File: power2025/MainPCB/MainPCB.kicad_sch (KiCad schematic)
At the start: 11 parts, among them Q1 SUD08P06-155L, U1 NCP167BMX330TBG

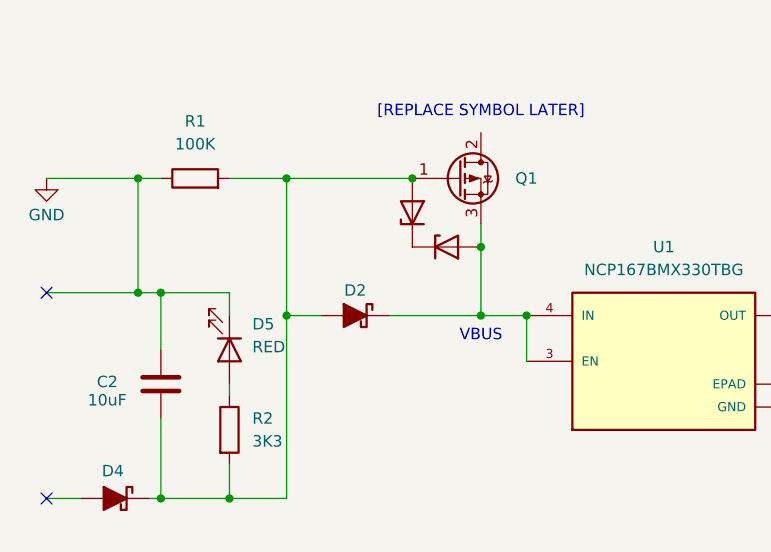
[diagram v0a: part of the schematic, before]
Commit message: Created symbol for CJ3139K mosfet
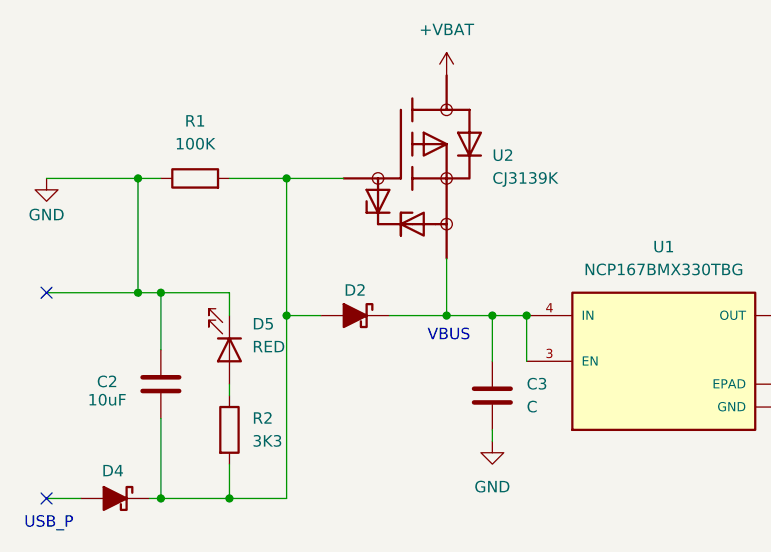
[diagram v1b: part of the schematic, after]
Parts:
- removed D1, D3: D_Zener, symbol Device:D_Zener
- removed Q1: SUD08P06-155L, Package_TO_SOT_SMD:TO-252-2, symbol Transistor_FET:SUD08P06-155L
- added C3: C, symbol Device:C
- added U2: CJ3139K, symbol Added Parts:CJ3139K
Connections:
- net GND: now also C3.2
- net at D2.1 (K), U1.3 (EN), U1.4 (IN): now also C3.1, U2. (S)
- net at C2.2, D2.2 (A), D4.1 (K)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: now also U2. (S)
- new net +VBAT: U2. (S)
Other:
- note added: "USB_P"
- note removed: "[REPLACE SYMBOL LATER]"

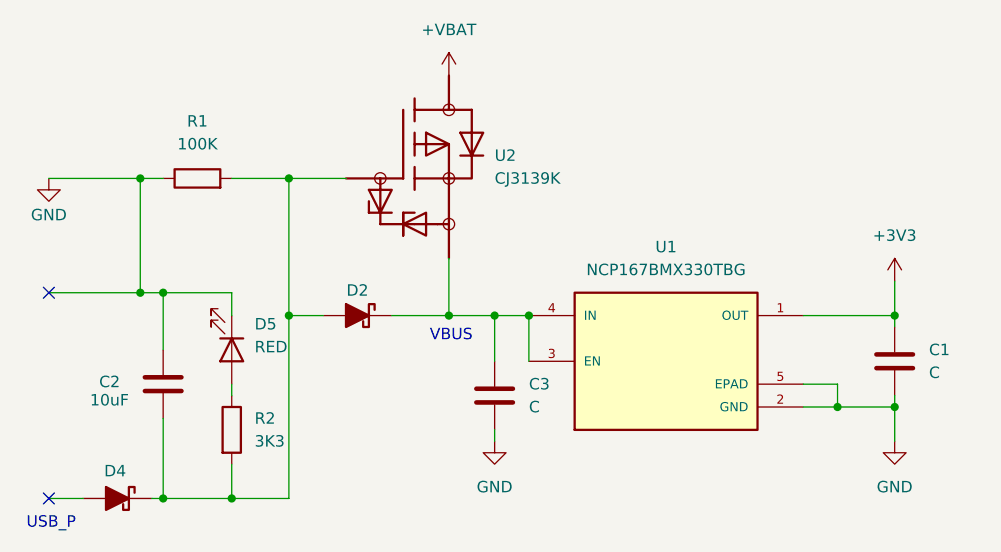
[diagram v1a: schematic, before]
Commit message: Added specific values for in/out capacitors
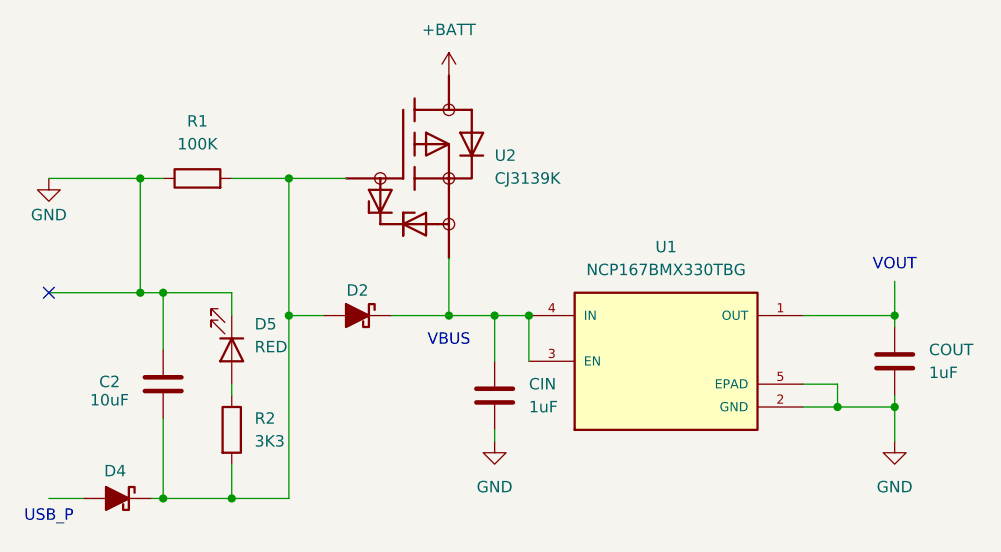
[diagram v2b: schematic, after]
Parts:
- CIN: renamed from C3; value C -> 1uF
- COUT: renamed from C1; value C -> 1uF
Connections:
- net +3V3: no longer names the net of COUT.1, U1.1 (OUT)
- net +VBAT renamed +BATT
- no-connect marks 2 -> 1
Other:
- note added: "VOUT"
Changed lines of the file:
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@@
 	(generator_version "9.0")
 	(paper "A4")
-	(text "USB_P"
-		(exclude_from_sim no)
-		(at 52.324 70.104 0)
+	(text "VOUT"
+		(exclude_from_sim no)
+		(at 146.05 41.402 0)
 		(effects
 			(font
 				(size 1.27 1.27)
-				(color 0 0 0 1)
 			)
 		)
@@
 	(text "VBUS"
 		(exclude_from_sim no)
-		(at 96.774 49.276 0)
+		(at 96.52 49.784 0)
 		(effects
 			(font
 				(size 1.27 1.27)
-				(color 0 0 0 1)
+			)
+		)
+	)
+	(text "USB_P\n"
+		(exclude_from_sim no)
+		(at 52.07 69.342 0)
+		(effects
+			(font
+				(size 1.27 1.27)
 			)
 		)
@@
 	(no_connect
 		(at 52.07 44.45)
-	)
-	(no_connect
-		(at 52.07 67.31)
 	)
 	(wire
@@
 		(dnp no)
 		(fields_autoplaced yes)
-		(property "Reference" "C1"
+		(property "Reference" "COUT"
 			(at 149.86 50.7999 0)
 			(effects
@@
 			)
 		)
-		(property "Value" "C"
+		(property "Value" "1uF"
 			(at 149.86 53.3399 0)
 			(effects
@@
 			(project ""
 				(path "/352d37ed-eb7c-4d4e-9251-f506b387d60c"
-					(reference "C1")
+					(reference "COUT")
 					(unit 1)
 				)
@@
 		(dnp no)
 		(fields_autoplaced yes)
-		(property "Reference" "#PWR04"
+		(property "Reference" "#PWR02"
 			(at 96.52 24.13 0)
 			(effects
@@
 			)
 		)
-		(property "Value" "+VBAT"
+		(property "Value" "+BATT"
 			(at 96.52 15.24 0)
 			(effects
@@
 			(project ""
 				(path "/352d37ed-eb7c-4d4e-9251-f506b387d60c"
-					(reference "#PWR04")
+					(reference "#PWR02")
 					(unit 1)
 				)
@@
 		(dnp no)
 		(fields_autoplaced yes)
-		(property "Reference" "C3"
+		(property "Reference" "CIN"
 			(at 105.41 54.6099 0)
 			(effects
@@
 			)
 		)
-		(property "Value" "C"
+		(property "Value" "1uF"
 			(at 105.41 57.1499 0)
 			(effects
@@
 			(project "MainPCB"
 				(path "/352d37ed-eb7c-4d4e-9251-f506b387d60c"
-					(reference "C3")
+					(reference "CIN")
 					(unit 1)
 				)
-			)
-		)
-	)
-	(symbol
-		(lib_id "power:+3V3")
-		(at 146.05 43.18 0)
-		(unit 1)
-		(exclude_from_sim no)
-		(in_bom yes)
-		(on_board yes)
-		(dnp no)
-		(fields_autoplaced yes)
-		(property "Reference" "#PWR02"
-			(at 146.05 46.99 0)
-			(effects
-				(font
-					(size 1.27 1.27)
-				)
-				(hide yes)
-			)
-		)
-		(property "Value" "+3V3"
-			(at 146.05 38.1 0)
-			(effects
-				(font
-					(size 1.27 1.27)
-				)
-			)
-		)
-		(property "Footprint" ""
-			(at 146.05 43.18 0)
-			(effects
-				(font
-					(size 1.27 1.27)
-				)
-				(hide yes)
-			)
-		)
-		(property "Datasheet" ""
-			(at 146.05 43.18 0)
-			(effects
-				(font
-					(size 1.27 1.27)
-				)
-				(hide yes)
-			)
-		)
-		(property "Description" "Power symbol creates a global label with name \"+3V3\""
-			(at 146.05 43.18 0)
-			(effects
-				(font
-					(size 1.27 1.27)
-				)
-				(hide yes)
-			)
-		)
-		(pin "1"
-		)
-		(instances
-			(project ""
-				(path "/352d37ed-eb7c-4d4e-9251-f506b387d60c"
-					(reference "#PWR02")
-					(unit 1)
-				)

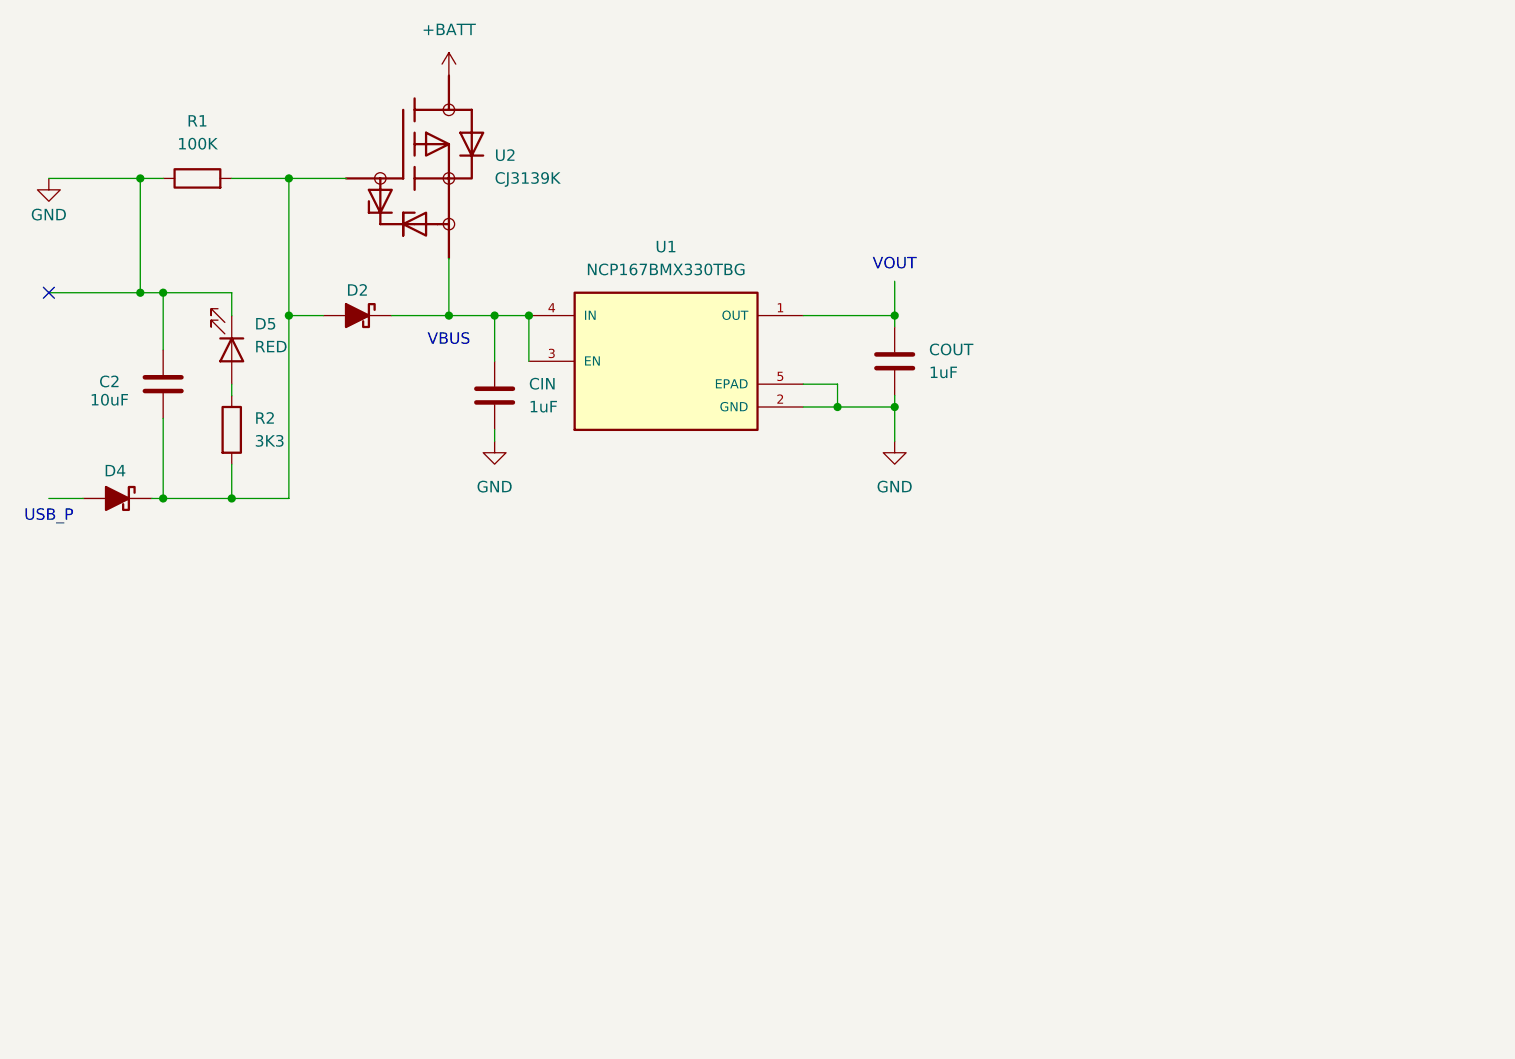
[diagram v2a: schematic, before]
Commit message: Added footprints
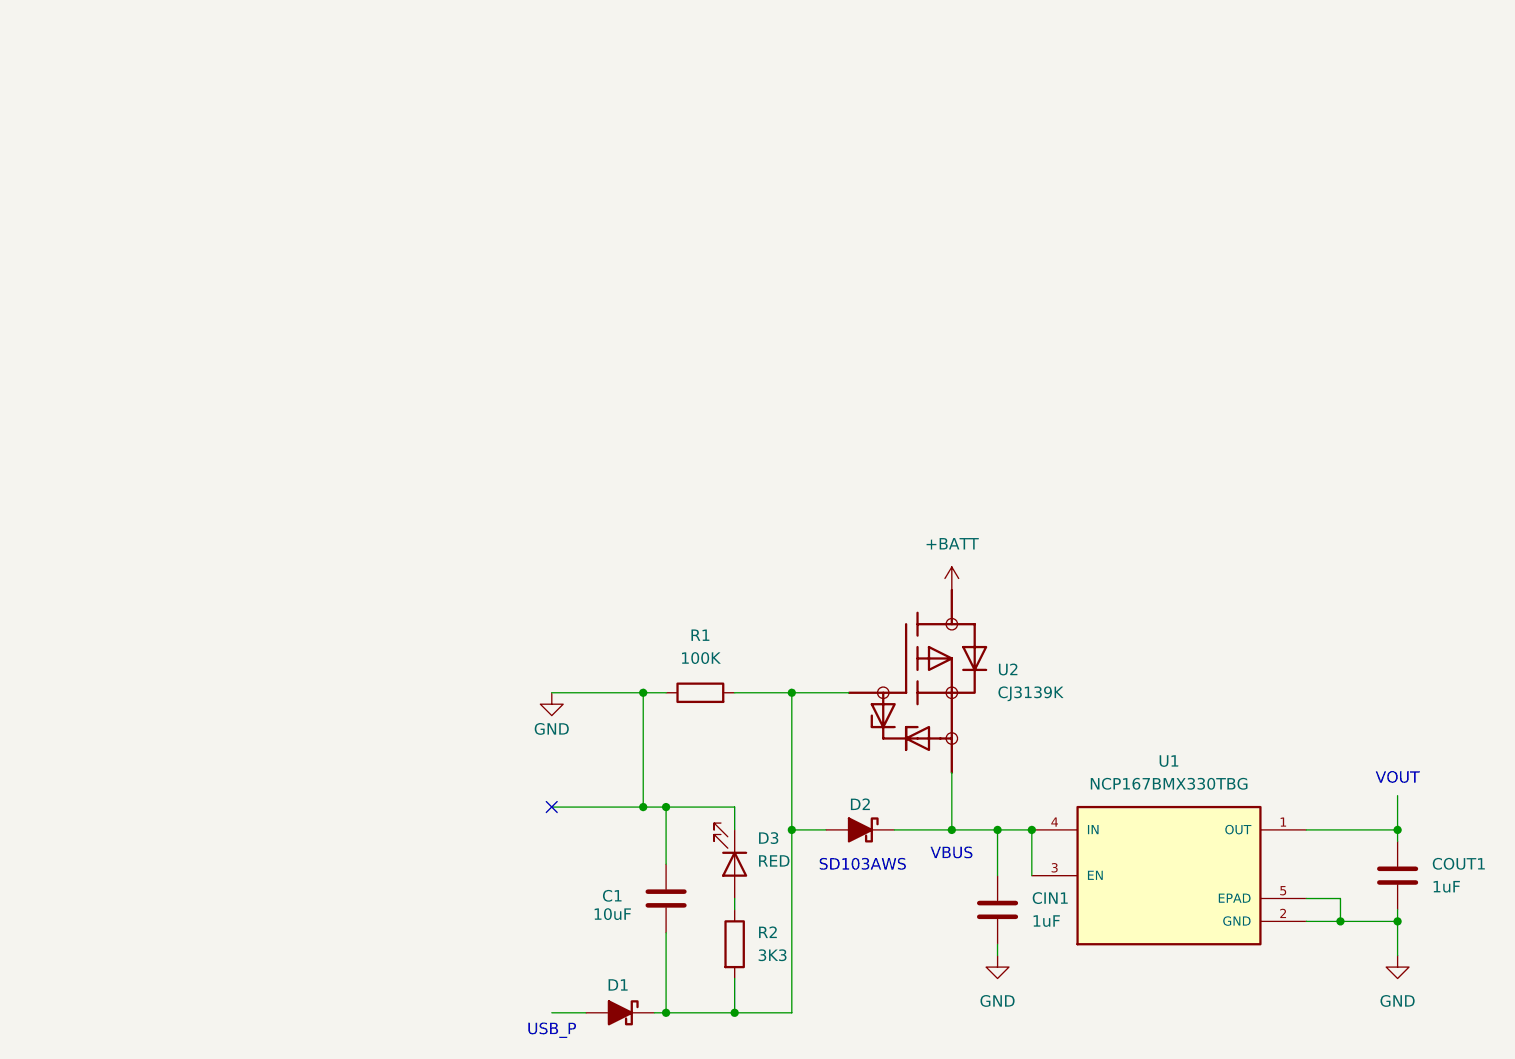
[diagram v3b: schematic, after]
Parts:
- C1: renamed from C2; footprint (none) -> Capacitor_SMD:CP_Elec_3x5.3
- CIN1: renamed from CIN; footprint (none) -> Capacitor_SMD:CP_Elec_3x5.3
- COUT1: renamed from COUT; footprint (none) -> Capacitor_SMD:CP_Elec_3x5.3
- D1: renamed from D4; footprint (none) -> Added Parts:SOD2513X120N
- D2: footprint (none) -> Added Parts:SOD2513X120N
- D3: renamed from D5; footprint (none) -> LED_SMD:LED-APA102-2020
- R1, R2: footprint (none) -> Resistor_SMD:R_0201_0603Metric
- U1: footprint NCP167BMX330TBG:VREG_NCP167BMX330TBG -> Added Parts:VREG_NCP167BMX330TBG
- U2: footprint (none) -> Added Parts:SOP65P210X110-6N
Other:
- note added: "SD103AWS"
- moved on the sheet: C1, CIN1, COUT1, D1, D2, D3, R1, R2, U1, U2
